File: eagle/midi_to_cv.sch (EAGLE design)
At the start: 74 parts, among them IC2 TL084P, IC3 TL084P, IC5 TL084P, U1 ATMEGA328P_PDIP, U2 MCP4822-E/P, U3 MCP4822-E/P, U4 MCP4822-E/P, U5 MCP4822-E/P

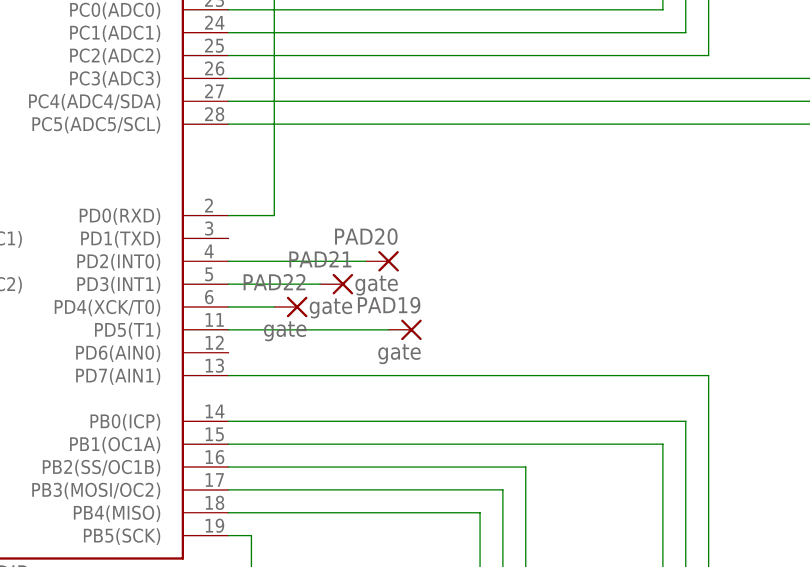
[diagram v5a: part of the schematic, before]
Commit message: moved parts onto board area
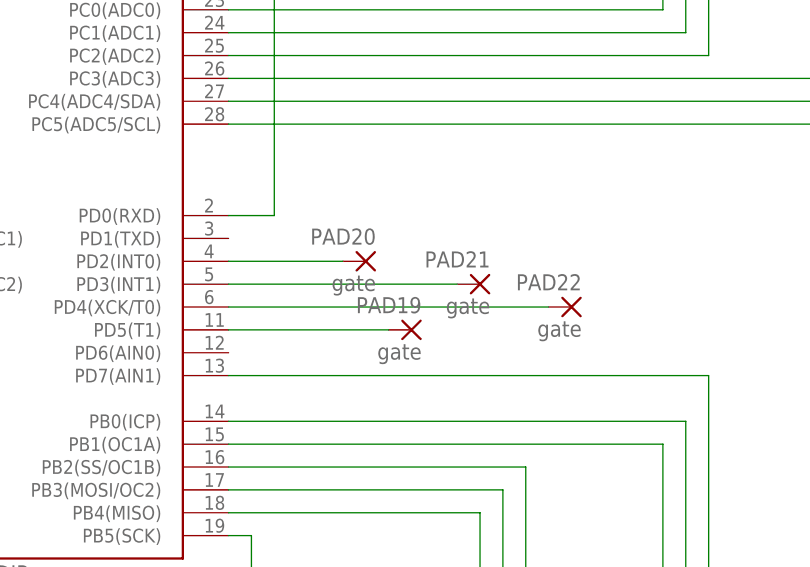
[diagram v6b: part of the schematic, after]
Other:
- moved on the sheet: PAD20, PAD21, PAD22
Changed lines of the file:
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@@
 <instance part="PAD18" gate="1" x="5.08" y="-73.66"/>
 <instance part="PAD19" gate="1" x="63.5" y="38.1" rot="MR0"/>
-<instance part="PAD20" gate="1" x="60.96" y="45.72" rot="MR0"/>
-<instance part="PAD21" gate="1" x="55.88" y="43.18" rot="MR0"/>
-<instance part="PAD22" gate="1" x="50.8" y="40.64" rot="MR0"/>
+<instance part="PAD20" gate="1" x="58.42" y="45.72" rot="MR0"/>
+<instance part="PAD21" gate="1" x="71.12" y="43.18" rot="MR0"/>
+<instance part="PAD22" gate="1" x="81.28" y="40.64" rot="MR0"/>
 <instance part="JP1" gate="A" x="45.72" y="-7.62"/>
 <instance part="GND5" gate="1" x="109.22" y="-86.36"/>
@@
 <segment>
 <pinref part="U1" gate="G$1" pin="PD2(INT0)"/>
-<wire x1="43.18" y1="45.72" x2="58.42" y2="45.72" width="0.1524" layer="91"/>
+<wire x1="43.18" y1="45.72" x2="55.88" y2="45.72" width="0.1524" layer="91"/>
 <pinref part="PAD20" gate="1" pin="P"/>
 </segment>
@@
 <segment>
 <pinref part="U1" gate="G$1" pin="PD3(INT1)"/>
-<wire x1="43.18" y1="43.18" x2="53.34" y2="43.18" width="0.1524" layer="91"/>
+<wire x1="43.18" y1="43.18" x2="68.58" y2="43.18" width="0.1524" layer="91"/>
 <pinref part="PAD21" gate="1" pin="P"/>
 </segment>
@@
 <segment>
 <pinref part="U1" gate="G$1" pin="PD4(XCK/T0)"/>
-<wire x1="43.18" y1="40.64" x2="48.26" y2="40.64" width="0.1524" layer="91"/>
+<wire x1="43.18" y1="40.64" x2="78.74" y2="40.64" width="0.1524" layer="91"/>
 <pinref part="PAD22" gate="1" pin="P"/>
 </segment>

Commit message: working to route the board
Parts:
- removed IC3, IC5: TL084P, linear:TL084P
- removed JP1: (no value), pinhead:PINHD-2X3
- added IC1, IC4, IC6, IC7: TL082P, linear:TL082P
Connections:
- net +12V: now also IC1P.V+, IC4P.V+, IC6P.V+, IC7P.V+; no longer IC3P.V+, IC5P.V+
- net -12V: now also IC1P.V-, IC4P.V-, IC6P.V-, IC7P.V-; no longer IC3P.V-, IC5P.V-
- net N$12: now also IC7A.-IN; no longer IC5B.-IN
- net N$16: now also IC1A.+IN; no longer IC3A.+IN
- net N$17: now also IC1A.OUT; no longer IC3A.OUT
- net N$18: now also IC1A.-IN; no longer IC3A.-IN
- net N$19: now also IC7B.OUT; no longer IC5D.OUT
- net N$20: now also IC7B.-IN; no longer IC5D.-IN
- net N$21: now also IC1B.OUT; no longer IC3C.OUT
- net N$22: now also IC1B.-IN; no longer IC3C.-IN
- net N$24: now also IC1B.+IN; no longer IC3C.+IN
- net N$26: now also IC4A.+IN; no longer IC3B.+IN
- net N$49: now also IC4A.OUT; no longer IC3B.OUT
- net N$50: now also IC4A.-IN; no longer IC3B.-IN
- net N$51: now also IC7B.+IN; no longer IC5D.+IN
- net N$52: now also IC4B.OUT; no longer IC3D.OUT
- net N$53: now also IC4B.-IN; no longer IC3D.-IN
- net N$54: now also IC4B.+IN; no longer IC3D.+IN
- net N$56: now also IC6A.+IN; no longer IC5A.+IN
- net N$57: now also IC6A.OUT; no longer IC5A.OUT
- net N$58: now also IC6A.-IN; no longer IC5A.-IN
- net N$59: now also IC6B.OUT; no longer IC5C.OUT
- net N$6: now also IC7A.+IN; no longer IC5B.+IN
- net N$60: now also IC6B.-IN; no longer IC5C.-IN
- net N$61: now also IC6B.+IN; no longer IC5C.+IN
- net N$9: now also IC7A.OUT; no longer IC5B.OUT

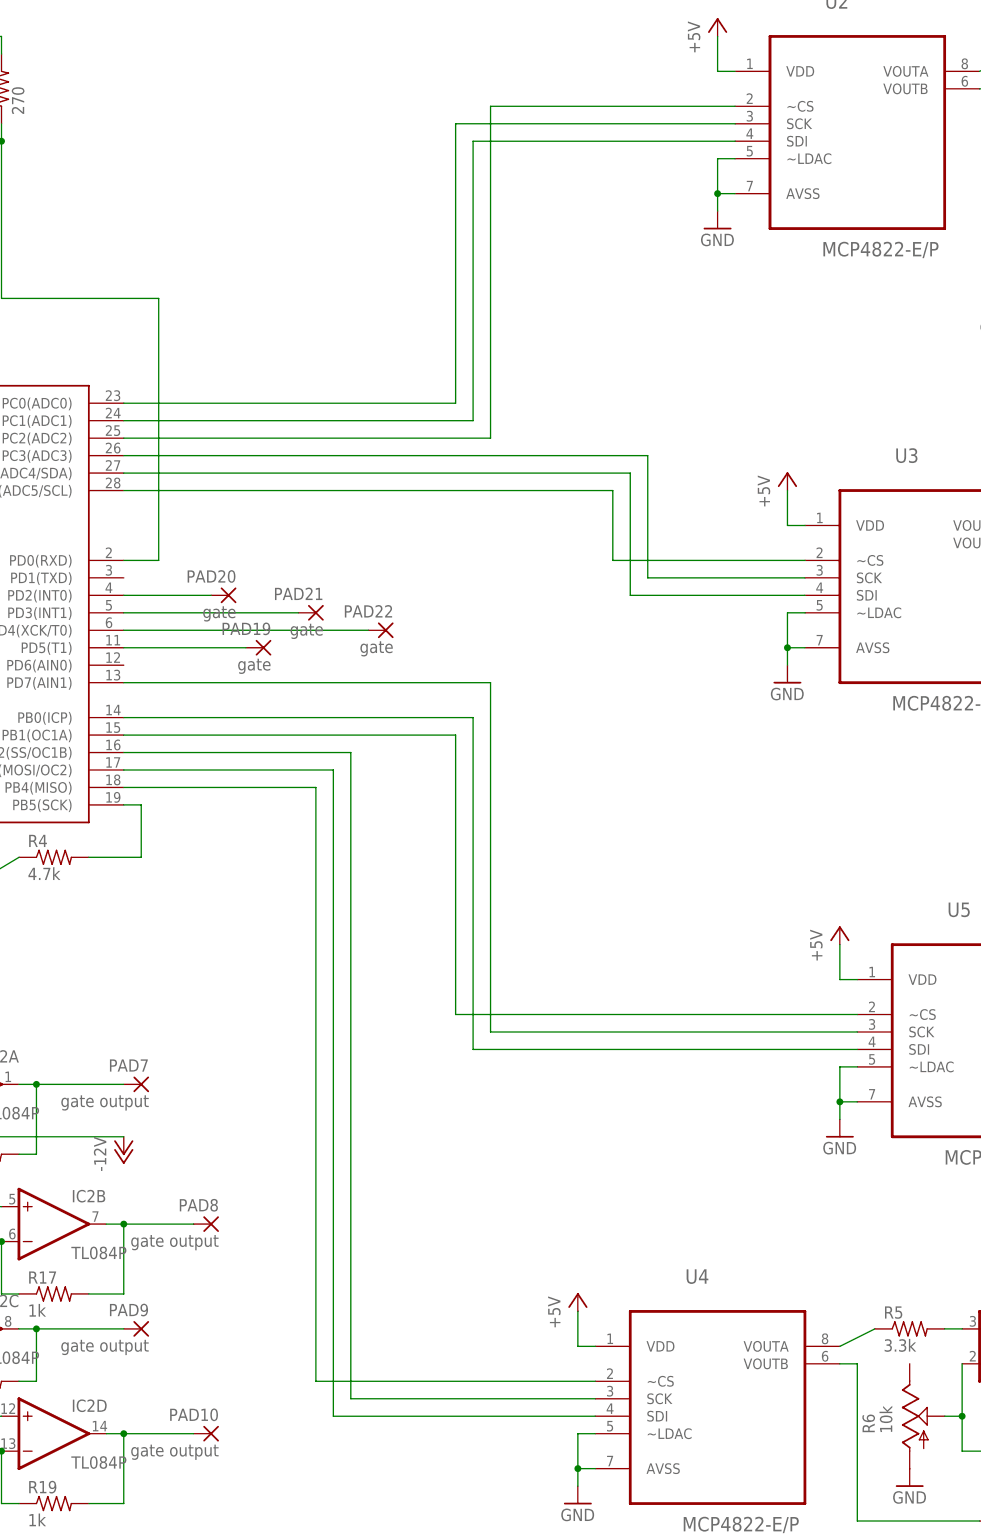
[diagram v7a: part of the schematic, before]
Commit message: swapped dac control lines and need to do so in software
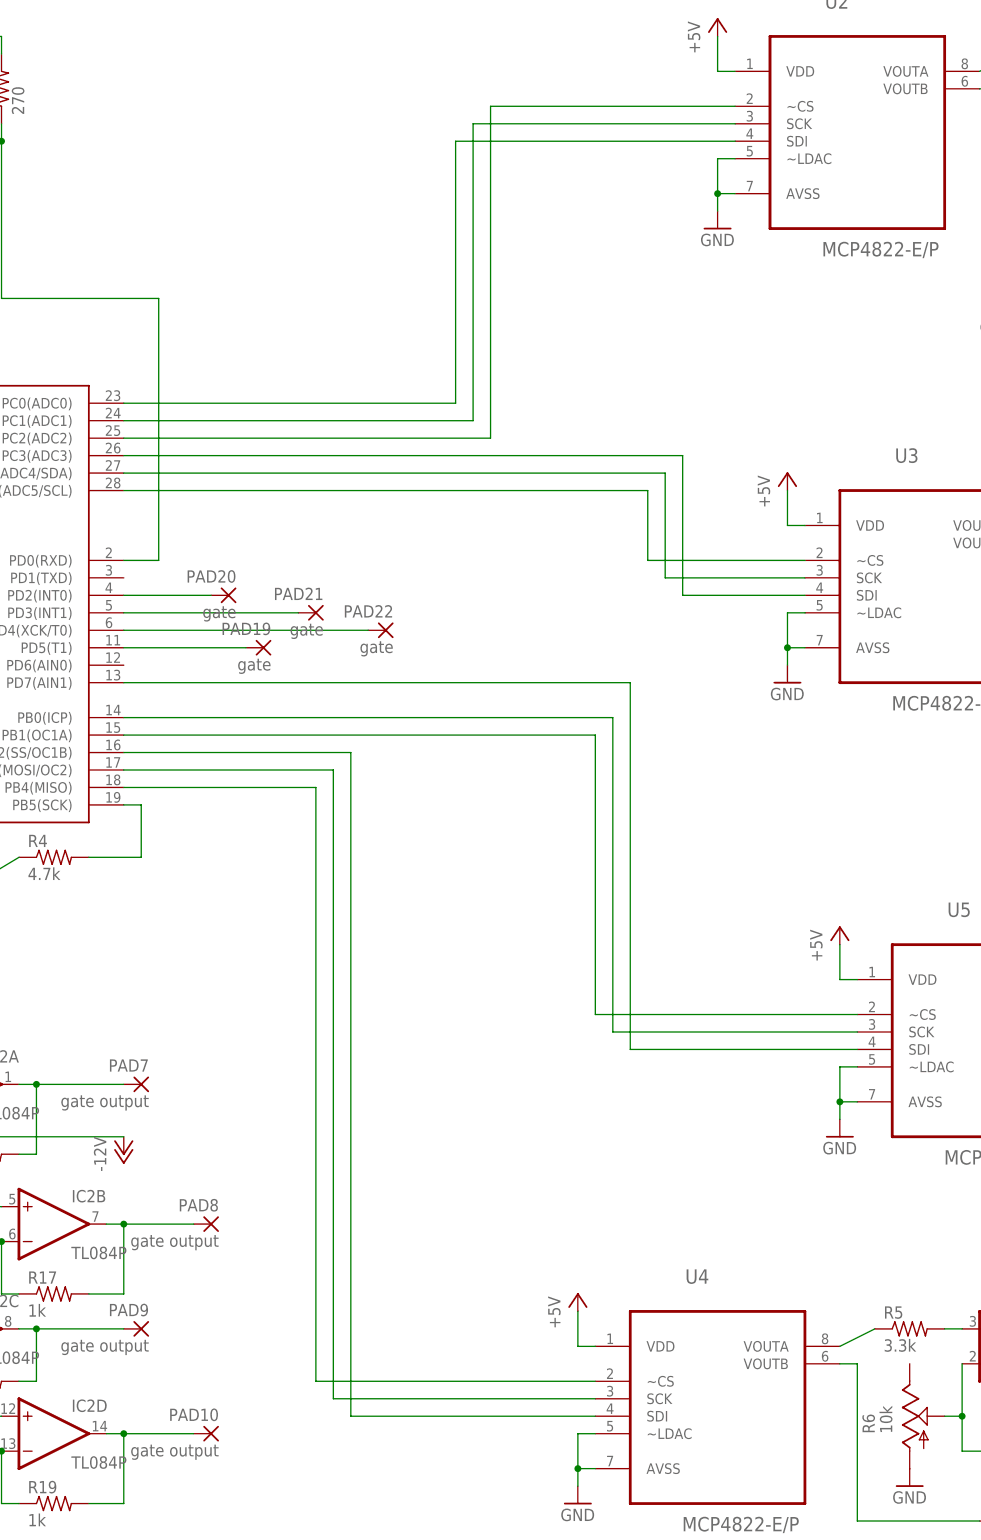
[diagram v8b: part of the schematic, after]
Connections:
- removed net N$23: U1.PB0(ICP), U5.SDI
- new net N$68: U1.PB0(ICP), U5.SCK
- net N$14: now also U4.SCK; no longer U4.SDI
- net N$15: now also U4.SDI; no longer U4.SCK
- net N$28: now also U5.SDI; no longer U5.SCK
- net N$62: now also U2.SDI; no longer U2.SCK
- net N$63: now also U2.SCK; no longer U2.SDI
- net N$65: now also U3.SDI; no longer U3.SCK
- net N$66: now also U3.SCK; no longer U3.SDI
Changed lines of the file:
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@@
 <segment>
 <pinref part="U1" gate="G$1" pin="PD7(AIN1)"/>
-<wire x1="43.18" y1="33.02" x2="96.52" y2="33.02" width="0.1524" layer="91"/>
-<wire x1="96.52" y1="33.02" x2="96.52" y2="-17.78" width="0.1524" layer="91"/>
-<pinref part="U5" gate="A" pin="SCK"/>
-<wire x1="96.52" y1="-17.78" x2="149.86" y2="-17.78" width="0.1524" layer="91"/>
-</segment>
-</net>
-<net name="N$23" class="0">
-<segment>
-<pinref part="U1" gate="G$1" pin="PB0(ICP)"/>
-<wire x1="43.18" y1="27.94" x2="93.98" y2="27.94" width="0.1524" layer="91"/>
-<wire x1="93.98" y1="27.94" x2="93.98" y2="-20.32" width="0.1524" layer="91"/>
+<wire x1="43.18" y1="33.02" x2="116.84" y2="33.02" width="0.1524" layer="91"/>
+<wire x1="116.84" y1="33.02" x2="116.84" y2="-20.32" width="0.1524" layer="91"/>
 <pinref part="U5" gate="A" pin="SDI"/>
-<wire x1="93.98" y1="-20.32" x2="149.86" y2="-20.32" width="0.1524" layer="91"/>
+<wire x1="116.84" y1="-20.32" x2="149.86" y2="-20.32" width="0.1524" layer="91"/>
 </segment>
 </net>
@@
 <segment>
 <pinref part="U1" gate="G$1" pin="PB1(OC1A)"/>
-<wire x1="43.18" y1="25.4" x2="91.44" y2="25.4" width="0.1524" layer="91"/>
-<wire x1="91.44" y1="25.4" x2="91.44" y2="-15.24" width="0.1524" layer="91"/>
+<wire x1="43.18" y1="25.4" x2="111.76" y2="25.4" width="0.1524" layer="91"/>
+<wire x1="111.76" y1="25.4" x2="111.76" y2="-15.24" width="0.1524" layer="91"/>
 <pinref part="U5" gate="A" pin="~CS"/>
-<wire x1="91.44" y1="-15.24" x2="149.86" y2="-15.24" width="0.1524" layer="91"/>
+<wire x1="111.76" y1="-15.24" x2="149.86" y2="-15.24" width="0.1524" layer="91"/>
 </segment>
 </net>
@@
 <pinref part="U1" gate="G$1" pin="PB3(MOSI/OC2)"/>
 <wire x1="43.18" y1="20.32" x2="73.66" y2="20.32" width="0.1524" layer="91"/>
-<wire x1="73.66" y1="20.32" x2="73.66" y2="-73.66" width="0.1524" layer="91"/>
-<pinref part="U4" gate="A" pin="SDI"/>
-<wire x1="73.66" y1="-73.66" x2="111.76" y2="-73.66" width="0.1524" layer="91"/>
+<pinref part="U4" gate="A" pin="SCK"/>
+<wire x1="111.76" y1="-71.12" x2="73.66" y2="-71.12" width="0.1524" layer="91"/>
+<wire x1="73.66" y1="-71.12" x2="73.66" y2="20.32" width="0.1524" layer="91"/>
 </segment>
 </net>
@@
 <pinref part="U1" gate="G$1" pin="PB2(SS/OC1B)"/>
 <wire x1="43.18" y1="22.86" x2="76.2" y2="22.86" width="0.1524" layer="91"/>
-<wire x1="76.2" y1="22.86" x2="76.2" y2="-71.12" width="0.1524" layer="91"/>
-<pinref part="U4" gate="A" pin="SCK"/>
-<wire x1="76.2" y1="-71.12" x2="111.76" y2="-71.12" width="0.1524" layer="91"/>
+<wire x1="76.2" y1="22.86" x2="76.2" y2="-73.66" width="0.1524" layer="91"/>
+<pinref part="U4" gate="A" pin="SDI"/>
+<wire x1="76.2" y1="-73.66" x2="111.76" y2="-73.66" width="0.1524" layer="91"/>
 </segment>
 </net>
@@
 <pinref part="U1" gate="G$1" pin="PC0(ADC0)"/>
 <wire x1="43.18" y1="73.66" x2="91.44" y2="73.66" width="0.1524" layer="91"/>
-<wire x1="91.44" y1="73.66" x2="91.44" y2="114.3" width="0.1524" layer="91"/>
-<pinref part="U2" gate="A" pin="SCK"/>
-<wire x1="91.44" y1="114.3" x2="132.08" y2="114.3" width="0.1524" layer="91"/>
+<wire x1="91.44" y1="73.66" x2="91.44" y2="111.76" width="0.1524" layer="91"/>
+<pinref part="U2" gate="A" pin="SDI"/>
+<wire x1="91.44" y1="111.76" x2="132.08" y2="111.76" width="0.1524" layer="91"/>
 </segment>
 </net>
@@
 <pinref part="U1" gate="G$1" pin="PC1(ADC1)"/>
 <wire x1="43.18" y1="71.12" x2="93.98" y2="71.12" width="0.1524" layer="91"/>
-<wire x1="93.98" y1="71.12" x2="93.98" y2="111.76" width="0.1524" layer="91"/>
-<pinref part="U2" gate="A" pin="SDI"/>
-<wire x1="93.98" y1="111.76" x2="132.08" y2="111.76" width="0.1524" layer="91"/>
+<pinref part="U2" gate="A" pin="SCK"/>
+<wire x1="132.08" y1="114.3" x2="93.98" y2="114.3" width="0.1524" layer="91"/>
+<wire x1="93.98" y1="114.3" x2="93.98" y2="71.12" width="0.1524" layer="91"/>
 </segment>
 </net>
@@
 <segment>
 <pinref part="U1" gate="G$1" pin="PC3(ADC3)"/>
-<wire x1="43.18" y1="66.04" x2="119.38" y2="66.04" width="0.1524" layer="91"/>
-<wire x1="119.38" y1="66.04" x2="119.38" y2="48.26" width="0.1524" layer="91"/>
+<wire x1="43.18" y1="66.04" x2="124.46" y2="66.04" width="0.1524" layer="91"/>
+<wire x1="124.46" y1="66.04" x2="124.46" y2="45.72" width="0.1524" layer="91"/>
+<pinref part="U3" gate="A" pin="SDI"/>
+<wire x1="124.46" y1="45.72" x2="142.24" y2="45.72" width="0.1524" layer="91"/>
+</segment>
+</net>
+<net name="N$66" class="0">
+<segment>
+<pinref part="U1" gate="G$1" pin="PC4(ADC4/SDA)"/>
+<wire x1="43.18" y1="63.5" x2="121.92" y2="63.5" width="0.1524" layer="91"/>
 <pinref part="U3" gate="A" pin="SCK"/>
-<wire x1="119.38" y1="48.26" x2="142.24" y2="48.26" width="0.1524" layer="91"/>
-</segment>
-</net>
-<net name="N$66" class="0">
-<segment>
-<pinref part="U1" gate="G$1" pin="PC4(ADC4/SDA)"/>
-<wire x1="43.18" y1="63.5" x2="116.84" y2="63.5" width="0.1524" layer="91"/>
-<wire x1="116.84" y1="63.5" x2="116.84" y2="45.72" width="0.1524" layer="91"/>
-<pinref part="U3" gate="A" pin="SDI"/>
-<wire x1="116.84" y1="45.72" x2="142.24" y2="45.72" width="0.1524" layer="91"/>
+<wire x1="142.24" y1="48.26" x2="121.92" y2="48.26" width="0.1524" layer="91"/>
+<wire x1="121.92" y1="48.26" x2="121.92" y2="63.5" width="0.1524" layer="91"/>
 </segment>
 </net>
@@
 <segment>
 <pinref part="U1" gate="G$1" pin="PC5(ADC5/SCL)"/>
-<wire x1="43.18" y1="60.96" x2="114.3" y2="60.96" width="0.1524" layer="91"/>
-<wire x1="114.3" y1="60.96" x2="114.3" y2="50.8" width="0.1524" layer="91"/>
+<wire x1="43.18" y1="60.96" x2="119.38" y2="60.96" width="0.1524" layer="91"/>
+<wire x1="119.38" y1="60.96" x2="119.38" y2="50.8" width="0.1524" layer="91"/>
 <pinref part="U3" gate="A" pin="~CS"/>
-<wire x1="114.3" y1="50.8" x2="142.24" y2="50.8" width="0.1524" layer="91"/>
-</segment>
-</net>
+<wire x1="119.38" y1="50.8" x2="142.24" y2="50.8" width="0.1524" layer="91"/>
+</segment>
+</net>
+<net name="N$68" class="0">
+<segment>
+<pinref part="U1" gate="G$1" pin="PB0(ICP)"/>
+<wire x1="43.18" y1="27.94" x2="114.3" y2="27.94" width="0.1524" layer="91"/>
+<pinref part="U5" gate="A" pin="SCK"/>
+<wire x1="149.86" y1="-17.78" x2="114.3" y2="-17.78" width="0.1524" layer="91"/>
+<wire x1="114.3" y1="-17.78" x2="114.3" y2="27.94" width="0.1524" layer="91"/>
+</segment>
+</net>
